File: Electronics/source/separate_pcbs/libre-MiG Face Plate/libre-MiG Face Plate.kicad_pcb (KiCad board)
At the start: 2 copper layers, 46.9 x 54.7 mm, 8 parts, among them J19 Conn_01x08, J20 Conn_01x03, SW1 SW_Push, SW16 SW_Push, SW17 SKRHABE010

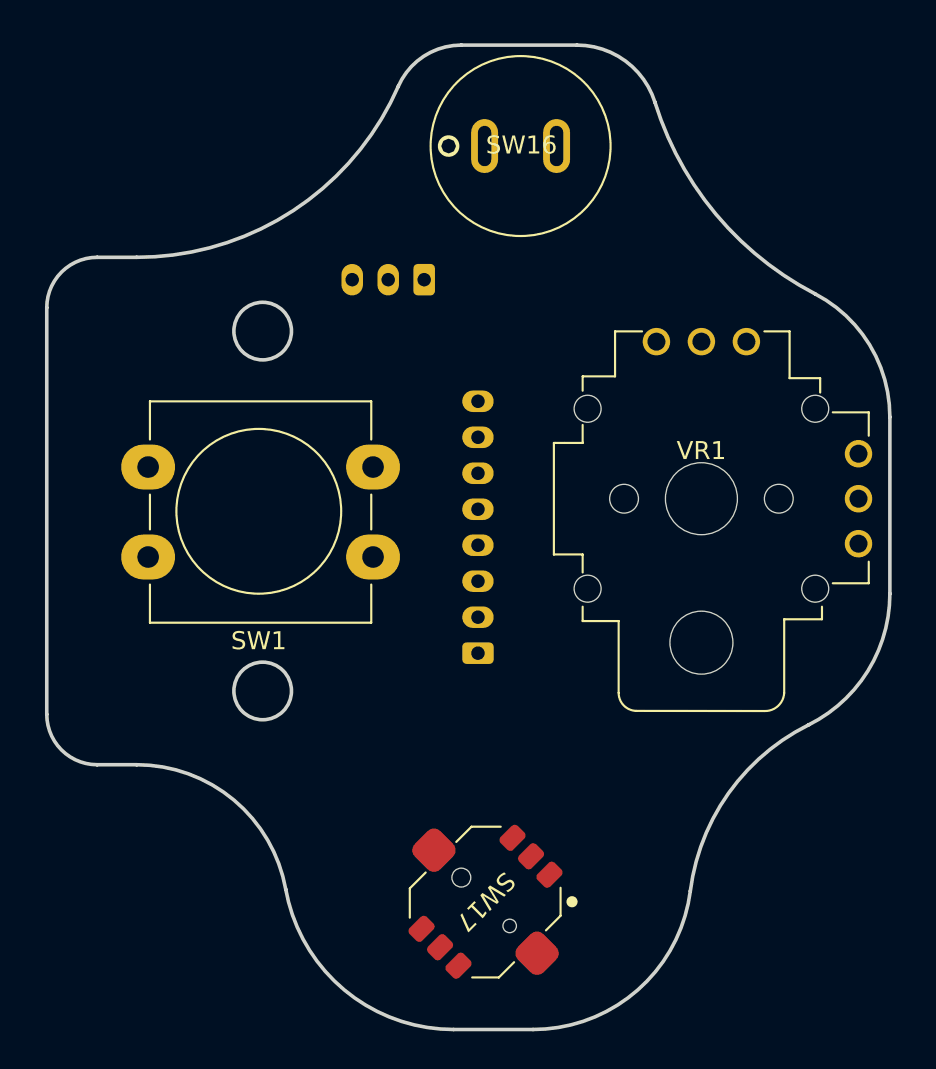
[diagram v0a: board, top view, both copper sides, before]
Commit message: added mechanical ignore
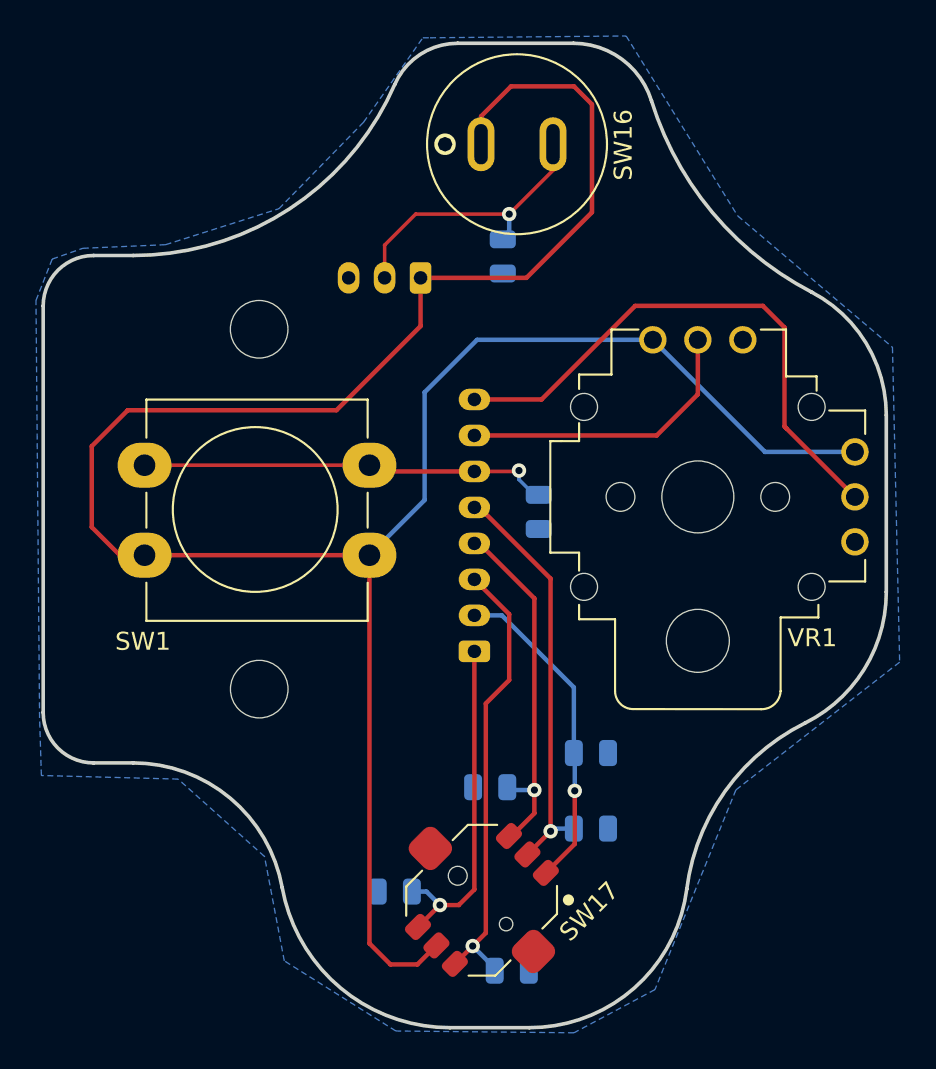
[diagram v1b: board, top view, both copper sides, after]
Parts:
- removed the REF** at (119.0, 150.9)
- removed the REF** at (119.0, 170.9)
- added C26: 100nF, Capacitor_SMD:C_0805_2012Metric, B.Cu at (137.2, 178.6)
- added C27: 100nF, Capacitor_SMD:C_0805_2012Metric, B.Cu at (137.2, 174.4)
- added C28: 100nF, Capacitor_SMD:C_0805_2012Metric, B.Cu at (131.6, 176.3)
- added C29: 100nF, Capacitor_SMD:C_0805_2012Metric, B.Cu at (134.3, 161.0)
- added C30: 100nF, Capacitor_SMD:C_0805_2012Metric, B.Cu at (132.3, 146.8)
- added C31: 100nF, Capacitor_SMD:C_0805_2012Metric, B.Cu at (132.8, 186.5)
- added C32: 100nF, Capacitor_SMD:C_0805_2012Metric, B.Cu at (126.3, 182.1)
- added REF**: MountingHole_3.2mm_M3, MountingHole:MountingHole_3.2mm_M3, F.Cu at (118.8, 150.8)
- added REF**: MountingHole_3.2mm_M3, MountingHole:MountingHole_3.2mm_M3, F.Cu at (118.8, 170.8)
- moved SW17 0.22 mm to (131.1, 182.6)
- moved VR1 0.22 mm to (143.1, 160.2)
- moved SW1 0.22 mm to (124.9, 163.4)
- moved J19 0.22 mm to (130.7, 168.7)
- moved SW16 0.22 mm to (133.1, 140.6)
- moved J20 0.22 mm to (127.7, 148.0)
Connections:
- J19 pad 1: /Face Plate/Axis1 -> /Face Plate/DirD
- J19 pad 2: /Face Plate/Axis2 -> /Face Plate/DirU
- J19 pad 3: /Face Plate/CenterButt -> /Face Plate/DirR
- J19 pad 4: /Face Plate/DirC -> /Face Plate/DirL
- J19 pad 5: /Face Plate/DirL -> /Face Plate/DirC
- J19 pad 6: /Face Plate/DirR -> /Face Plate/CenterButt
- J19 pad 7: /Face Plate/DirU -> /Face Plate/Axis2
- J19 pad 8: /Face Plate/DirD -> /Face Plate/Axis1
- SW1 pad 1: unconnected-(SW1-Pad1) -> +3V3
- SW1 pad 2: unconnected-(SW1-Pad2) -> /Face Plate/CenterButt
- SW16 pad 1: unconnected-(SW16-Pad1) -> +3V3
- SW16 pad 2: unconnected-(SW16-Pad2) -> /Face Plate/BigRed
- SW17 pad 2: /Face Plate/CenterButt -> /Face Plate/DirC
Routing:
- net +3V3: track 0.00 -> 134.4 mm
- net /Face Plate/Axis1: track 0.00 -> 30.9 mm
- net /Face Plate/DirR: track 0.00 -> 25.3 mm, vias 0 -> 1
- net /Face Plate/CenterButt: track 0.00 -> 22.9 mm, vias 0 -> 1
- net /Face Plate/DirC: track 0.00 -> 22.9 mm, vias 0 -> 1
- net /Face Plate/DirL: track 0.00 -> 19.9 mm, vias 0 -> 1
- net /Face Plate/DirD: track 0.00 -> 19.1 mm, vias 0 -> 1
- net /Face Plate/DirU: track 0.00 -> 18.2 mm, vias 0 -> 1
- net /Face Plate/Axis2: track 0.00 -> 16.4 mm
- net /Face Plate/BigRed: track 0.00 -> 15.9 mm, vias 0 -> 1
- added copper zone on B.Cu, net GND
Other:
- outline, holes or cut-outs redrawn
